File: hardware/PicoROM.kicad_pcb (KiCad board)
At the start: 6 copper layers, 42.2 x 17.8 mm, 56 parts, among them J1 USB_C_Receptacle_USB2.0, J2 External Reset, J3 Conn_01x16, J4 Conn_01x16, J5 Conn_01x05_Pin, U1 AP2112K-3.3, U10 74LVCH8T245, U2 W25Q16JVUXIQ, U3 RP2040, U4 74LVCH245, U5 74LVCH245, U7 TCA5405RUGR, U8 74AHCT1G126, U9 74LVCH245, Y1 445C25D12M00000

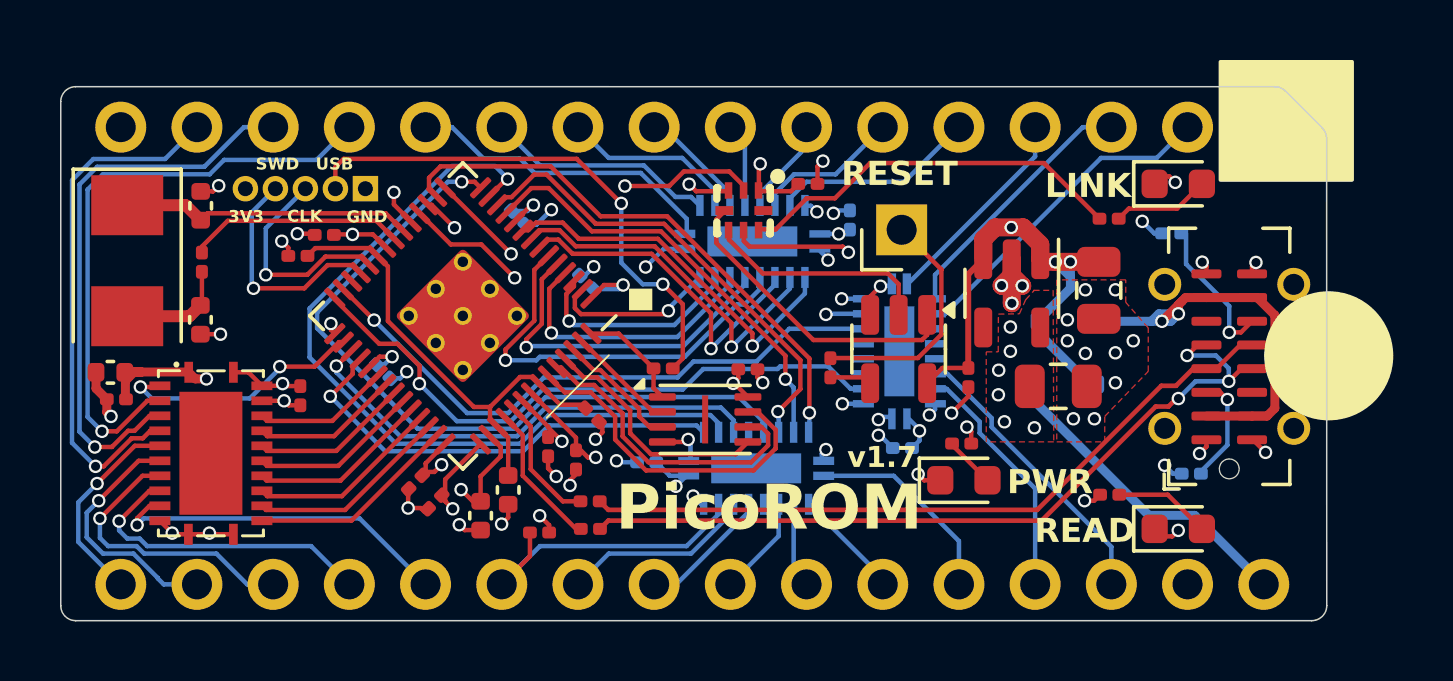
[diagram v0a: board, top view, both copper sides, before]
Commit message: Redesigned ROM emulator.
Changes from the original:
- 4 layer PCB (not 6)
- different level shifters
- 0402 resistors and caps
- reworked ~OE for level shifters
- added fiducials
- different pin solution

TODO:
- make sure USB is impedance matched
- review board outline, tweak if necessary
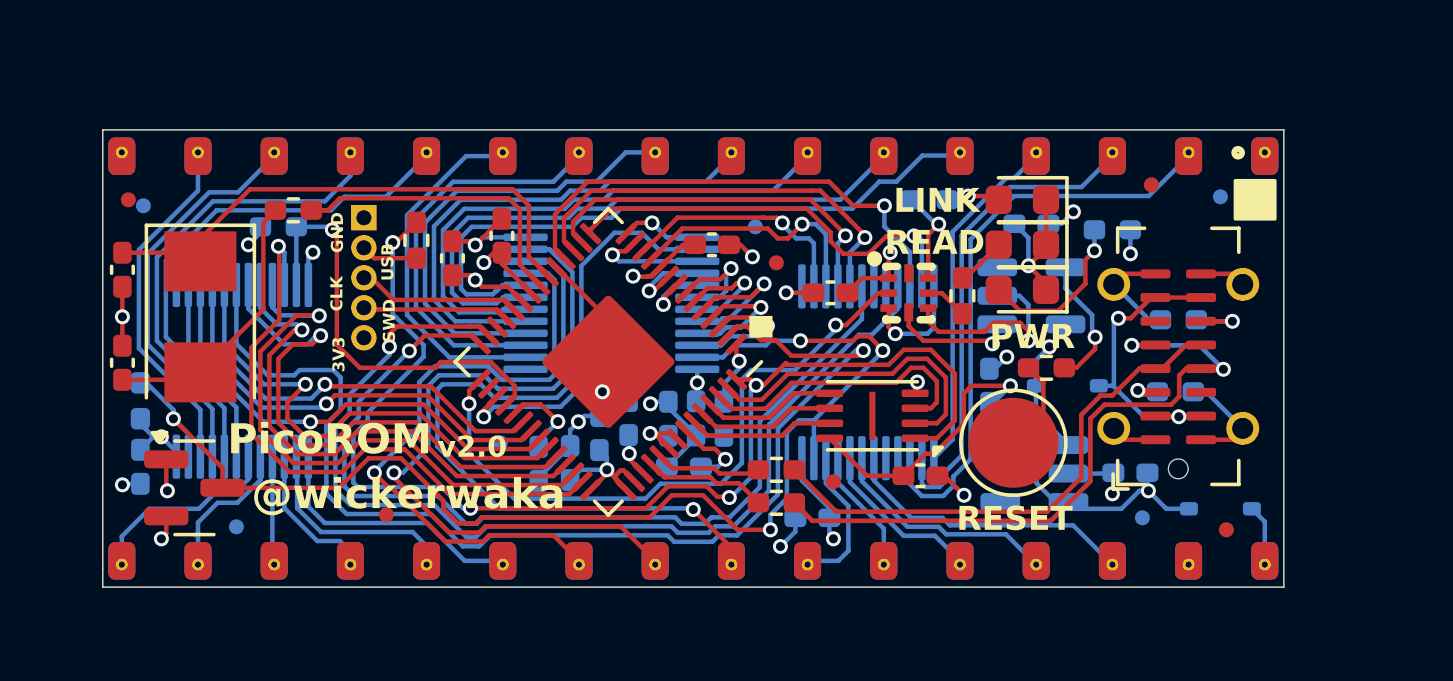
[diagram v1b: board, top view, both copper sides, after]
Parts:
- removed C14, C15, C21, C22: 100n, Capacitor_SMD:C_0201_0603Metric
- removed C25: 1u, Capacitor_SMD:C_0402_1005Metric
- removed J3, J4: Conn_01x16, Connector_PinHeader_2.54mm:PinHeader_1x16_P2.54mm_Vertical
- removed U10: 74LVCH8T245, RP2040_minimal:DHVQFN24_L5.5-W3.5-P0.50-BL-EP
- removed U9: 74LVCH245, RP2040_minimal:V-QFN4525-20_L4.5-W2.5-P0.50-BL
- added FID1: Fiducial, UNIC:Fiducial_0.5mm_Mask1mm, B.Cu at (88.1, 70.3)
- added FID10: Fiducial, UNIC:Fiducial_0.5mm_Mask1mm, B.Cu at (118.3, 70.0)
- added FID11: Fiducial, UNIC:Fiducial_0.5mm_Mask1mm, B.Cu at (105.4, 60.4)
- added FID12: Fiducial, UNIC:Fiducial_0.5mm_Mask1mm, F.Cu at (118.6, 59.0)
- added FID2: Fiducial, UNIC:Fiducial_0.5mm_Mask1mm, B.Cu at (96.9, 67.5)
- added FID3: Fiducial, UNIC:Fiducial_0.5mm_Mask1mm, B.Cu at (85.0, 59.6)
- added FID4: Fiducial, UNIC:Fiducial_0.5mm_Mask1mm, F.Cu at (84.5, 59.5)
- added FID5: Fiducial, UNIC:Fiducial_0.5mm_Mask1mm, F.Cu at (121.1, 70.5)
- added FID6: Fiducial, UNIC:Fiducial_0.5mm_Mask1mm, B.Cu at (120.9, 59.4)
- added FID7: Fiducial, UNIC:Fiducial_0.5mm_Mask1mm, F.Cu at (93.1, 70.0)
- added FID8: Fiducial, UNIC:Fiducial_0.5mm_Mask1mm, F.Cu at (108.0, 68.8)
- added FID9: Fiducial, UNIC:Fiducial_0.5mm_Mask1mm, F.Cu at (106.1, 61.5)
- added J6: Conn_02x16_Counter_Clockwise, UNIC:DIP-32_pin_header, F.Cu at (103.4, 64.7)
- added Q1: 2N7002, Package_TO_SOT_SMD:SOT-23, F.Cu at (86.7, 69.0)
- added R12: 5.1k, Resistor_SMD:R_0402_1005Metric_Pad0.72x0.64mm_HandSolder, B.Cu at (119.5, 63.5)
- added U6: 74CBTD3861, Package_SO:TSSOP-24_4.4x5mm_P0.4mm, B.Cu at (100.6, 62.9)
- C1, C4: footprint Capacitor_SMD:C_0805_2012Metric -> Capacitor_SMD:C_0402_1005Metric_Pad0.74x0.62mm_HandSolder; moved to B.Cu
- C10, C8: footprint Capacitor_SMD:C_0402_1005Metric -> Capacitor_SMD:C_0402_1005Metric_Pad0.74x0.62mm_HandSolder; moved to B.Cu
- C11, C12, C13, C17, C19, C20, C24, C6, C9: value 100n -> 1u; footprint Capacitor_SMD:C_0201_0603Metric -> Capacitor_SMD:C_0402_1005Metric_Pad0.74x0.62mm_HandSolder
- C16: value 100n -> 1u; footprint Capacitor_SMD:C_0201_0603Metric -> Capacitor_SMD:C_0402_1005Metric_Pad0.74x0.62mm_HandSolder; moved to F.Cu
- C18, C23, C5, C7: value 100n -> 1u; footprint Capacitor_SMD:C_0201_0603Metric -> Capacitor_SMD:C_0402_1005Metric_Pad0.74x0.62mm_HandSolder; moved to B.Cu
- C2, C3: footprint Capacitor_SMD:C_0402_1005Metric -> Capacitor_SMD:C_0402_1005Metric_Pad0.74x0.62mm_HandSolder
- J2: footprint Connector_PinHeader_2.54mm:PinHeader_1x01_P2.54mm_Vertical -> TestPoint:TestPoint_Pad_D3.0mm
- R1, R10, R2, R3, R6: footprint Resistor_SMD:R_0201_0603Metric -> Resistor_SMD:R_0402_1005Metric_Pad0.72x0.64mm_HandSolder
- R11: value 100k -> 1k; footprint Resistor_SMD:R_0201_0603Metric -> Resistor_SMD:R_0402_1005Metric_Pad0.72x0.64mm_HandSolder
- R4: value 27 -> 1k; footprint Resistor_SMD:R_0201_0603Metric -> Resistor_SMD:R_0402_1005Metric_Pad0.72x0.64mm_HandSolder; moved to B.Cu
- R5: value 1k -> 27; footprint Resistor_SMD:R_0201_0603Metric -> Resistor_SMD:R_0402_1005Metric_Pad0.72x0.64mm_HandSolder
- R7: value 5.1k -> 100k; footprint Resistor_SMD:R_0201_0603Metric -> Resistor_SMD:R_0402_1005Metric_Pad0.72x0.64mm_HandSolder
- R8: value 1k -> 10k; footprint Resistor_SMD:R_0201_0603Metric -> Resistor_SMD:R_0402_1005Metric_Pad0.72x0.64mm_HandSolder; moved to B.Cu
- R9: footprint Resistor_SMD:R_0201_0603Metric -> Resistor_SMD:R_0402_1005Metric_Pad0.72x0.64mm_HandSolder; moved to B.Cu
- U1, U8: moved to B.Cu
- U4, U5: value 74LVCH245 -> 74CBTD3861; footprint RP2040_minimal:V-QFN4525-20_L4.5-W2.5-P0.50-BL -> Package_SO:TSSOP-24_4.4x5mm_P0.4mm
- moved R7 29.8 mm to (89.5, 60.4), turned to 180 degrees
- moved C23 27.8 mm to (117.9, 68.5), turned to 180 degrees
- moved R8 23.0 mm to (84.9, 66.2)
- moved R5 20.4 mm to (106.1, 68.5), turned to 0 degrees
- moved R4 20.1 mm to (117.3, 60.5), turned to 0 degrees
- moved C1 19.5 mm to (98.2, 68.2)
- moved U5 17.4 mm to (88.3, 65.2), turned to -90 degrees
- moved C9 16.2 mm to (110.9, 68.7), turned to 0 degrees
- moved C18 16.1 mm to (100.2, 67.2), turned to 90 degrees
- moved C11 15.2 mm to (107.9, 62.5), turned to 180 degrees
- moved C17 15.1 mm to (84.9, 68.3), turned to -90 degrees
- moved R1 13.4 mm to (90.0, 59.8)
- moved C24 11.7 mm to (113.2, 65.7), turned to 90 degrees
- moved C4 11.2 mm to (104.4, 66.8), turned to -90 degrees
- moved D2 10.8 mm to (114.3, 61.0), turned to 180 degrees
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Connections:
- C1 pad 1: +5V -> +3V3
- C17 pad 1: +3V3 -> +5V
- C18 pad 1: +5V -> +3V3
- C19 pad 1: +3V3 -> +5V
- C2 pad 1: /XIN -> GND
- C2 pad 2: GND -> Net-(C2-Pad2)
- C20 pad 1: +3V3 -> +5V
- C23 pad 1: +3V3 -> +5V
- C3 pad 1: Net-(C3-Pad1) -> GND
- C3 pad 2: GND -> /XIN
- C5 pad 1: +3V3 -> +5V
- R1 pad 1: /QSPI_SS -> Net-(C2-Pad2)
- R1 pad 2: /~{USB_BOOT} -> /XOUT
- R10 pad 1: Net-(D2-A) -> Net-(R10-Pad1)
- R10 pad 2: /INFO_LED1 -> /EXT_RESET
- R11 pad 1: /~{PIN_CE} -> /~{USB_BOOT}
- R11 pad 2: +3V3 -> /QSPI_SS
- R2 pad 1: Net-(D3-A) -> Net-(D2-A)
- R2 pad 2: /INFO_LED2 -> /INFO_LED1
- R3 pad 1: /USB_D+ -> Net-(U3-USB_DM)
- R3 pad 2: Net-(U3-USB_DP) -> /USB_D-
- R4 pad 1: /USB_D- -> Net-(D1-A)
- R4 pad 2: Net-(U3-USB_DM) -> +3V3
- R5 pad 1: /XOUT -> Net-(U3-USB_DP)
- R5 pad 2: Net-(C3-Pad1) -> /USB_D+
- R6 pad 1: GND -> Net-(J1-CC1)
- R6 pad 2: Net-(J1-CC1) -> GND
- R7 pad 1: GND -> /~{CE}
- R7 pad 2: Net-(J1-CC2) -> +3V3
- R8 pad 1: /EXT_RESET -> /~{BUF_EN}
- R8 pad 2: Net-(R8-Pad2) -> +5V
- R9 pad 1: Net-(D1-A) -> Net-(D3-A)
- R9 pad 2: +3V3 -> /INFO_LED2
- U3 pad 30: /~{BUF_OE} -> unconnected-(U3-GPIO19-Pad30)
- U4 pad 1: GND -> unconnected-(U4-NC-Pad1)
- U4 pad 10: GND -> /A15
- U4 pad 11: /PIN_A12 -> /A12
- U4 pad 12: /PIN_A15 -> GND
- U4 pad 13: /PIN_A16 -> /PIN_A12
- U4 pad 14: unconnected-(U4-B4-Pad14) -> /PIN_A15
- U4 pad 15: unconnected-(U4-B3-Pad15) -> /PIN_A16
- U4 pad 17: /PIN_A17 -> unconnected-(U4-B6-Pad17)
- U4 pad 18: /PIN_A14 -> /PIN_A17
- U4 pad 19: GND -> /PIN_A14
- U4 pad 2: /A14 -> /A9
- U4 pad 20: +3V3 -> /PIN_A13
- U4 pad 21: (no net) -> /PIN_A8
- U4 pad 3: /A17 -> /A8
- U4 pad 4: unconnected-(U4-A2-Pad4) -> /A13
- U4 pad 5: unconnected-(U4-A3-Pad5) -> /A14
- U4 pad 6: unconnected-(U4-A4-Pad6) -> /A17
- U4 pad 7: /A16 -> unconnected-(U4-A6-Pad7)
- U4 pad 8: /A15 -> unconnected-(U4-A7-Pad8)
- U4 pad 9: /A12 -> /A16
- U5 pad 1: GND -> unconnected-(U5-NC-Pad1)
- U5 pad 10: GND -> /D7
- U5 pad 11: /PIN_A13 -> /~{CE}
- U5 pad 12: /PIN_A8 -> GND
- U5 pad 13: /PIN_A9 -> /~{PIN_CE}
- U5 pad 14: /PIN_A11 -> /PIN_D7
- U5 pad 15: unconnected-(U5-B3-Pad15) -> /PIN_D6
- U5 pad 16: /~{PIN_OE} -> /PIN_D5
- U5 pad 17: /PIN_A10 -> /PIN_D4
- U5 pad 18: /~{PIN_CE} -> /PIN_D3
- U5 pad 19: GND -> /PIN_A0
- U5 pad 2: /~{CE} -> /D2
- U5 pad 20: +3V3 -> /PIN_D0
- U5 pad 21: (no net) -> /PIN_D1
- U5 pad 3: /A10 -> /D1
- U5 pad 4: /~{OE} -> /D0
- U5 pad 5: unconnected-(U5-A3-Pad5) -> /D3
- U5 pad 6: /A11 -> /A0
- U5 pad 7: /A9 -> /D4
- U5 pad 8: /A8 -> /D5
- U5 pad 9: /A13 -> /D6
- U8 pad 4: Net-(R8-Pad2) -> Net-(R10-Pad1)
- Y1 pad 2: Net-(C3-Pad1) -> Net-(C2-Pad2)
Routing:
- net +3V3: track 32.1 -> 97.1 mm, vias 23 -> 11
- net /~{BUF_EN}: track 0.00 -> 42.6 mm, vias 0 -> 4
- net /QSPI_SS: track 3.64 -> 39.3 mm, vias 0 -> 4
- net /A0: track 5.53 -> 38.0 mm
- net /A10: track 26.9 -> 3.83 mm
- net /A11: track 25.3 -> 2.72 mm
- net +5V: track 52.2 -> 73.9 mm, vias 4 -> 6
- net /PIN_A11: track 3.35 -> 24.1 mm, vias 0 -> 1
- net /~{PIN_OE}: track 4.40 -> 23.6 mm, vias 0 -> 1
- net /~{USB_BOOT}: track 17.9 -> 1.89 mm, vias 2 -> 0
- net /INFO_LED1: track 16.6 -> 1.42 mm, vias 2 -> 0
- net /PIN_A6: track 4.92 -> 20.1 mm
- net /PIN_A5: track 3.27 -> 18.4 mm
- net /PIN_A7: track 6.87 -> 21.8 mm
- net /PIN_A10: track 6.43 -> 21.1 mm, vias 0 -> 1
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- added copper zone on In2.Cu, net +1V1
- added copper zone on In2.Cu, net +5V
- removed copper zone on F.Cu, net +3V3
- removed copper zone on F.Cu, net GND
- removed copper zone on In4.Cu, net GND
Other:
- board size 42.2 x 17.8 mm -> 39.4 x 15.2 mm
- copper layers 6 -> 4
- rule pad_to_mask_clearance: 0.051 -> 0
- board text added: "v2.0"
- board text removed: "v1.7"
